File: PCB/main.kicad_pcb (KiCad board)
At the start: 2 copper layers, 82.5 x 58.4 mm, 39 parts, among them CON1 BARREL_JACK, P1 JUMPER_LEFT, P2 LEFT, P3 JUMPER_RIGHT, P4 RIGHT, Q1 3904, Q2 3904, Q3 3904, Q4 3904, SW1 12x12_PUSHBUTTON_SPST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

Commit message: pcb powa!
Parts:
- added REF**: Logo1, myparts:Logo1, F.Cu at (127.0, 52.8)
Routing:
- added copper zone on B.Cu, net GND

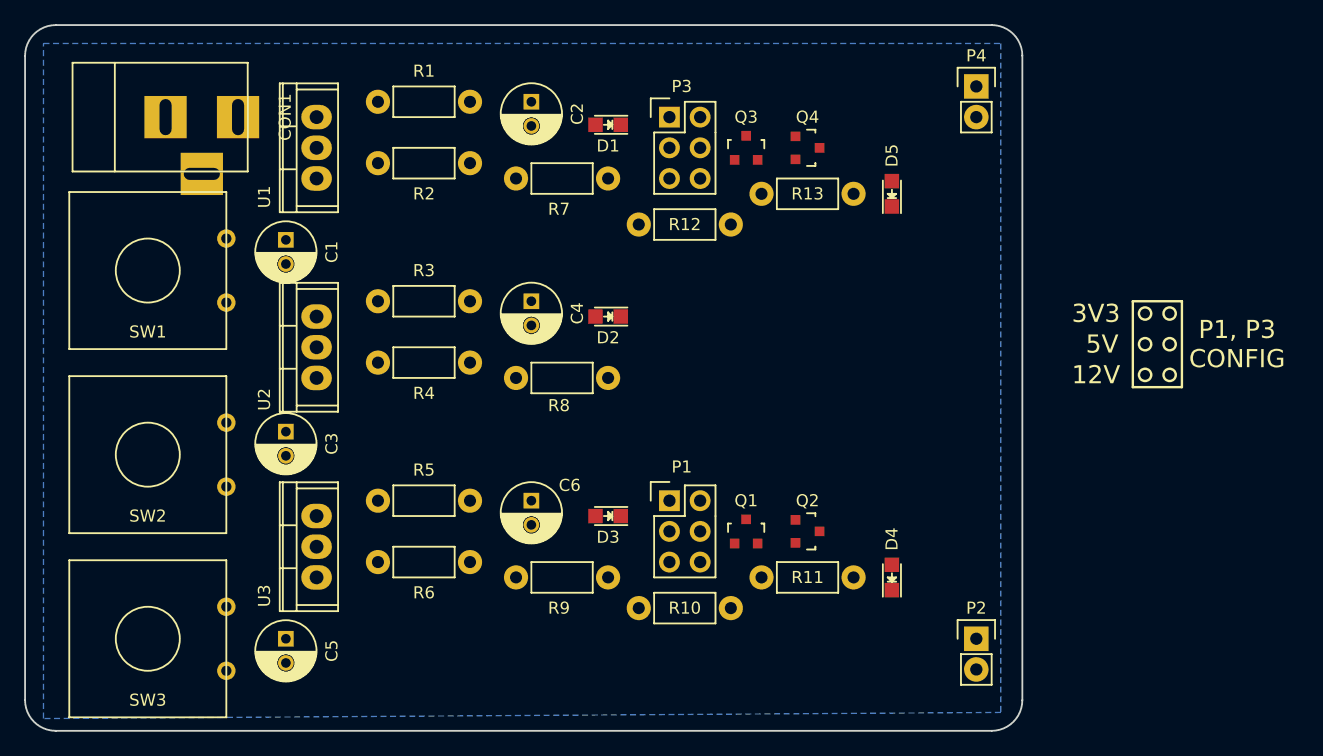
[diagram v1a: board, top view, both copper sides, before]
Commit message: smaller pcb
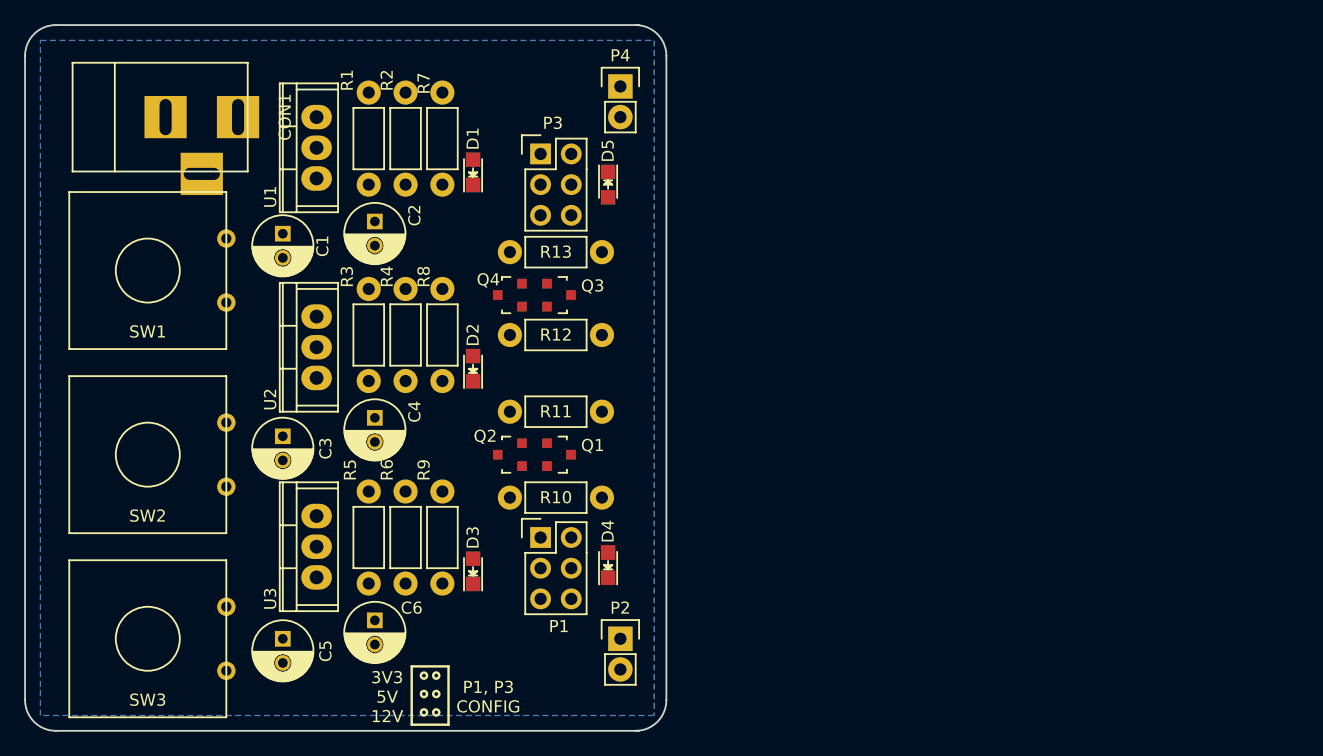
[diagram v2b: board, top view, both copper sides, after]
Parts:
- removed REF**: Logo1, myparts:Logo1
- moved P2 29.5 mm to (102.6, 71.1)
- moved P4 29.5 mm to (102.6, 25.4)
- moved Q4 27.5 mm to (93.5, 42.7), turned to 90 degrees
- moved Q2 25.4 mm to (93.5, 55.9), turned to 90 degrees
- moved D4 23.5 mm to (101.6, 65.0)
- moved D5 23.5 mm to (101.6, 33.5), turned to 270 degrees
- moved R12 20.4 mm to (93.5, 46.0), turned to 0 degrees
- moved Q3 19.7 mm to (97.5, 42.7), turned to 270 degrees
- moved R11 19.0 mm to (101.1, 52.3), turned to 180 degrees
- moved Q1 16.7 mm to (97.5, 55.9), turned to 270 degrees
- moved C6 16.3 mm to (82.3, 69.6)
- moved C2 16.3 mm to (82.3, 36.6)
- moved C4 16.2 mm to (82.3, 52.8)
- moved R13 14.1 mm to (101.1, 39.1), turned to 180 degrees
- moved R10 14.1 mm to (93.5, 59.4)
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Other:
- board size 82.5 x 58.4 mm -> 53.1 x 58.4 mm
- board text added: "3V3 5V 12V"
- board text removed: "12V"
- board text removed: "3V3"
- board text removed: "5V"

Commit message: edge cut fix
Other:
- outline, holes or cut-outs redrawn
- board text added: "+ -"
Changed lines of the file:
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@@
     (area 53.264999 20.244999 106.501001 78.815001)
     (thickness 1.524)
-    (drawings 21)
+    (drawings 23)
     (tracks 0)
     (zones 0)
@@
       (net 6 "Net-(C5-Pad1)"))
   )
+  (gr_text "+\n-" (at 105.156 26.416) (layer F.SilkS)
+    (effects (font (size 1.5 1.5) (thickness 0.3)))
+  )
+  (gr_text "+\n-" (at 105.156 72.39) (layer F.SilkS)
+    (effects (font (size 1.5 1.5) (thickness 0.3)))
+  )
+  (gr_line (start 53.34 22.86) (end 53.34 76.2) (angle 90) (layer Edge.Cuts) (width 0.15))
+  (gr_line (start 106.426 76.2) (end 106.426 22.86) (angle 90) (layer Edge.Cuts) (width 0.15))
+  (gr_line (start 55.88 78.74) (end 103.886 78.74) (angle 90) (layer Edge.Cuts) (width 0.15))
+  (gr_line (start 55.88 20.32) (end 103.886 20.32) (angle 90) (layer Edge.Cuts) (width 0.15))
   (gr_text "P1, P3\nCONFIG" (at 91.694 75.946) (layer F.SilkS)
     (effects (font (size 1 1) (thickness 0.2)))
@@
     (effects (font (size 1 1) (thickness 0.2)))
   )
-  (gr_line (start 55.88 78.74) (end 104.14 78.74) (angle 90) (layer Edge.Cuts) (width 0.15))
-  (gr_line (start 106.426 76.2) (end 106.426 22.86) (angle 90) (layer Edge.Cuts) (width 0.15))
-  (gr_line (start 55.88 20.32) (end 104.14 20.32) (angle 90) (layer Edge.Cuts) (width 0.15))
   (gr_text "Breadboard Power Supply v0.1\nBy : Yannick Gagne" (at 60.452 54.864 90) (layer B.SilkS)
     (effects (font (size 1.5 1.5) (thickness 0.3)) (justify mirror))
   )
-  (gr_line (start 53.34 22.86) (end 53.34 76.2) (angle 90) (layer Edge.Cuts) (width 0.15))
   (gr_arc (start 103.886 22.86) (end 103.886 20.32) (angle 90) (layer Edge.Cuts) (width 0.15))
   (gr_arc (start 103.886 76.2) (end 106.426 76.2) (angle 90) (layer Edge.Cuts) (width 0.15))

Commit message: output pins
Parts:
- moved P4 2.54 mm to (102.6, 27.9), turned to 180 degrees
- moved P2 2.54 mm to (102.6, 73.7), turned to 180 degrees
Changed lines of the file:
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@@
   (layers
     (0 F.Cu signal)
-    (31 B.Cu signal hide)
+    (31 B.Cu signal)
     (34 B.Paste user)
     (35 F.Paste user)
@@
       (effects (font (size 1 1) (thickness 0.15)))
     )
-    (fp_text value JUMPER_LEFT (at 1.016 8.89) (layer F.Fab) hide
+    (fp_text value JUMPER_LEFT (at 0 8.89) (layer F.Fab) hide
       (effects (font (size 1 1) (thickness 0.15)))
     )
@@
   )
   (module Pin_Headers:Pin_Header_Straight_1x02 (layer F.Cu)
-    (at 102.616 71.12)
+    (at 102.616 73.66 180)
     (descr "Through hole pin header")
     (tags "pin header")
-    (fp_text reference P2 (at 0 -2.54) (layer F.SilkS)
-      (effects (font (size 1 1) (thickness 0.15)))
-    )
-    (fp_text value LEFT (at 0 5.08) (layer F.Fab) hide
+    (fp_text reference P2 (at 0 -2.54 180) (layer F.SilkS)
+      (effects (font (size 1 1) (thickness 0.15)))
+    )
+    (fp_text value LEFT (at 0 5.08 180) (layer F.Fab) hide
       (effects (font (size 1 1) (thickness 0.15)))
     )
@@
     (fp_line (start -1.27 1.27) (end -1.27 3.81) (layer F.SilkS) (width 0.15))
     (fp_line (start -1.27 3.81) (end 1.27 3.81) (layer F.SilkS) (width 0.15))
-    (pad 1 thru_hole rect (at 0 0) (size 2.032 2.032) (drill 1.016) (layers *.Cu *.Mask F.SilkS)
+    (pad 1 thru_hole rect (at 0 0 180) (size 2.032 2.032) (drill 1.016) (layers *.Cu *.Mask F.SilkS)
       (net 15 "Net-(P1-Pad2)"))
-    (pad 2 thru_hole oval (at 0 2.54) (size 2.032 2.032) (drill 1.016) (layers *.Cu *.Mask F.SilkS)
+    (pad 2 thru_hole oval (at 0 2.54 180) (size 2.032 2.032) (drill 1.016) (layers *.Cu *.Mask F.SilkS)
       (net 2 GND))
     (model Pin_Headers.3dshapes/Pin_Header_Straight_1x02.wrl
@@
   )
   (module Pin_Headers:Pin_Header_Straight_1x02 (layer F.Cu)
-    (at 102.616 25.4)
+    (at 102.616 27.94 180)
     (descr "Through hole pin header")
     (tags "pin header")
-    (fp_text reference P4 (at 0 -2.54) (layer F.SilkS)
-      (effects (font (size 1 1) (thickness 0.15)))
-    )
-    (fp_text value RIGHT (at 0 5.588) (layer F.Fab) hide
+    (fp_text reference P4 (at 0 -2.54 180) (layer F.SilkS)
+      (effects (font (size 1 1) (thickness 0.15)))
+    )
+    (fp_text value RIGHT (at 0 5.588 180) (layer F.Fab) hide
       (effects (font (size 1 1) (thickness 0.15)))
     )
@@
     (fp_line (start -1.27 1.27) (end -1.27 3.81) (layer F.SilkS) (width 0.15))
     (fp_line (start -1.27 3.81) (end 1.27 3.81) (layer F.SilkS) (width 0.15))
-    (pad 1 thru_hole rect (at 0 0) (size 2.032 2.032) (drill 1.016) (layers *.Cu *.Mask F.SilkS)
+    (pad 1 thru_hole rect (at 0 0 180) (size 2.032 2.032) (drill 1.016) (layers *.Cu *.Mask F.SilkS)
       (net 16 "Net-(P3-Pad2)"))
-    (pad 2 thru_hole oval (at 0 2.54) (size 2.032 2.032) (drill 1.016) (layers *.Cu *.Mask F.SilkS)
+    (pad 2 thru_hole oval (at 0 2.54 180) (size 2.032 2.032) (drill 1.016) (layers *.Cu *.Mask F.SilkS)
       (net 2 GND))
     (model Pin_Headers.3dshapes/Pin_Header_Straight_1x02.wrl
@@
       (net 6 "Net-(C5-Pad1)"))
   )
-  (gr_text "+\n-" (at 105.156 26.416) (layer F.SilkS)
+  (gr_text "+\n-" (at 105.156 26.67 180) (layer F.SilkS)
     (effects (font (size 1.5 1.5) (thickness 0.3)))
   )
-  (gr_text "+\n-" (at 105.156 72.39) (layer F.SilkS)
+  (gr_text "+\n-" (at 105.156 72.39 180) (layer F.SilkS)
     (effects (font (size 1.5 1.5) (thickness 0.3)))
   )

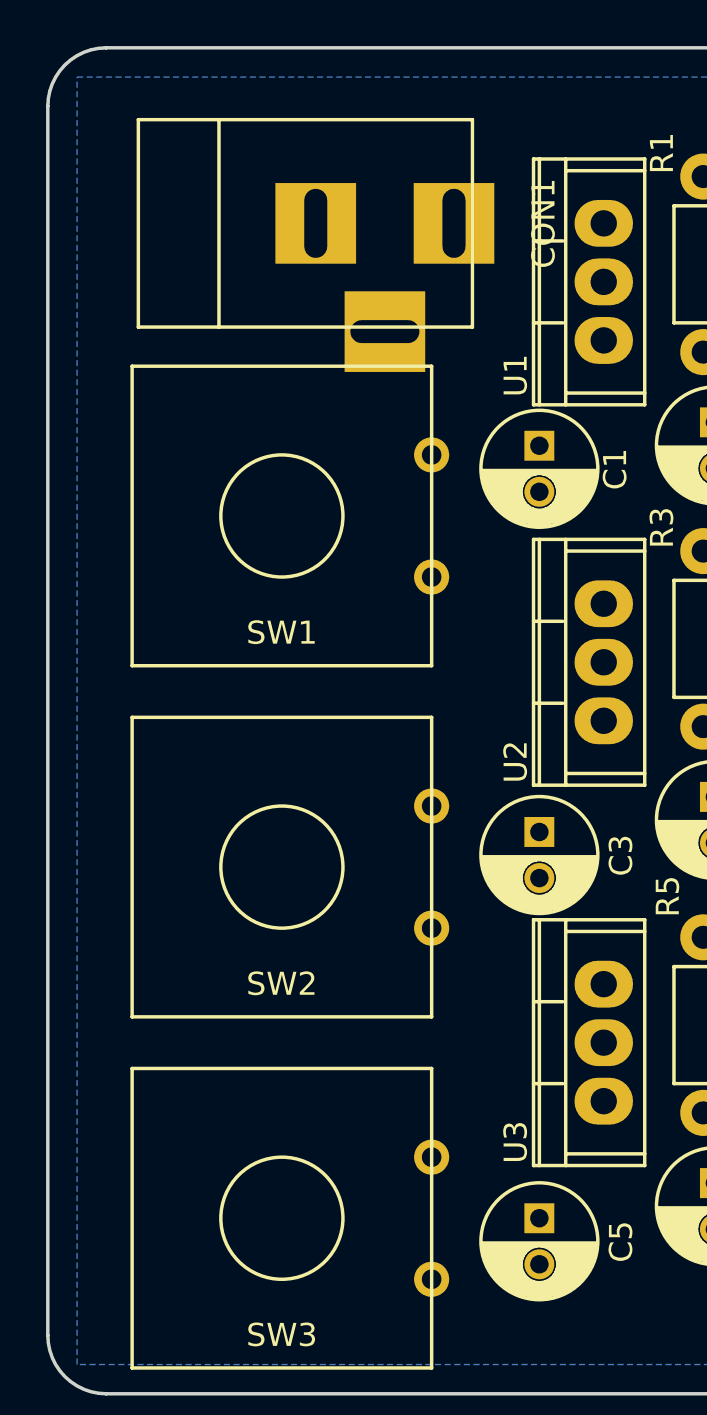
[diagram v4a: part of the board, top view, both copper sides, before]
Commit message: added to top silk screen
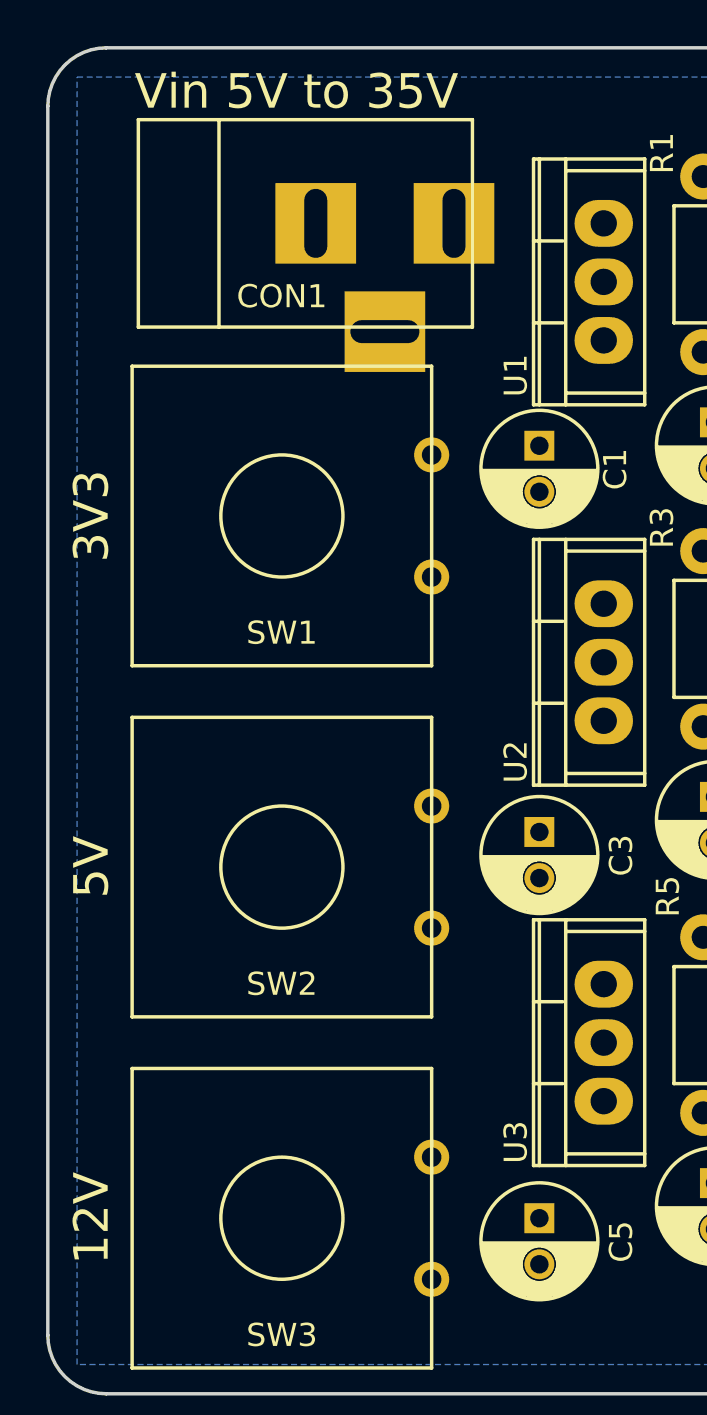
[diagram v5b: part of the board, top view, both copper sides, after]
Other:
- board text added: "12V"
- board text added: "3V3"
- board text added: "5V"
- board text added: "Vin 5V to 35V"
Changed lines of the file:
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@@
     (area 53.264999 20.244999 106.501001 78.815001)
     (thickness 1.524)
-    (drawings 23)
+    (drawings 28)
     (tracks 0)
     (zones 0)
@@
   (layers
     (0 F.Cu signal)
-    (31 B.Cu signal)
+    (31 B.Cu signal hide)
     (34 B.Paste user)
     (35 F.Paste user)
@@
     (descr "DC Barrel Jack")
     (tags "Power Jack")
-    (fp_text reference CON1 (at 10.09904 0 90) (layer F.SilkS)
-      (effects (font (size 1 1) (thickness 0.15)))
-    )
-    (fp_text value BARREL_JACK (at 1.27 -2.54) (layer F.Fab)
+    (fp_text reference CON1 (at -1.27 3.175 180) (layer F.SilkS)
+      (effects (font (size 1 1) (thickness 0.15)))
+    )
+    (fp_text value BARREL_JACK (at 1.27 -2.54) (layer F.Fab) hide
       (effects (font (size 1 1) (thickness 0.15)))
     )
@@
       (net 6 "Net-(C5-Pad1)"))
   )
+  (dimension 48.26 (width 0.3) (layer F.SilkS)
+    (gr_text "48,260 mm" (at 115.65 49.53 270) (layer F.SilkS)
+      (effects (font (size 1.5 1.5) (thickness 0.3)))
+    )
+    (feature1 (pts (xy 108.585 73.66) (xy 117 73.66)))
+    (feature2 (pts (xy 108.585 25.4) (xy 117 25.4)))
+    (crossbar (pts (xy 114.3 25.4) (xy 114.3 73.66)))
+    (arrow1a (pts (xy 114.3 73.66) (xy 113.713579 72.533496)))
+    (arrow1b (pts (xy 114.3 73.66) (xy 114.886421 72.533496)))
+    (arrow2a (pts (xy 114.3 25.4) (xy 113.713579 26.526504)))
+    (arrow2b (pts (xy 114.3 25.4) (xy 114.886421 26.526504)))
+  )
+  (gr_text "Vin 5V to 35V" (at 64.135 22.225) (layer F.SilkS)
+    (effects (font (size 1.5 1.5) (thickness 0.3)))
+  )
+  (gr_text 12V (at 55.245 71.12 90) (layer F.SilkS)
+    (effects (font (size 1.5 1.5) (thickness 0.3)))
+  )
+  (gr_text 5V (at 55.245 55.88 90) (layer F.SilkS)
+    (effects (font (size 1.5 1.5) (thickness 0.3)))
+  )
+  (gr_text 3V3 (at 55.245 40.64 90) (layer F.SilkS)
+    (effects (font (size 1.5 1.5) (thickness 0.3)))
+  )
   (gr_text "+\n-" (at 105.156 26.67 180) (layer F.SilkS)

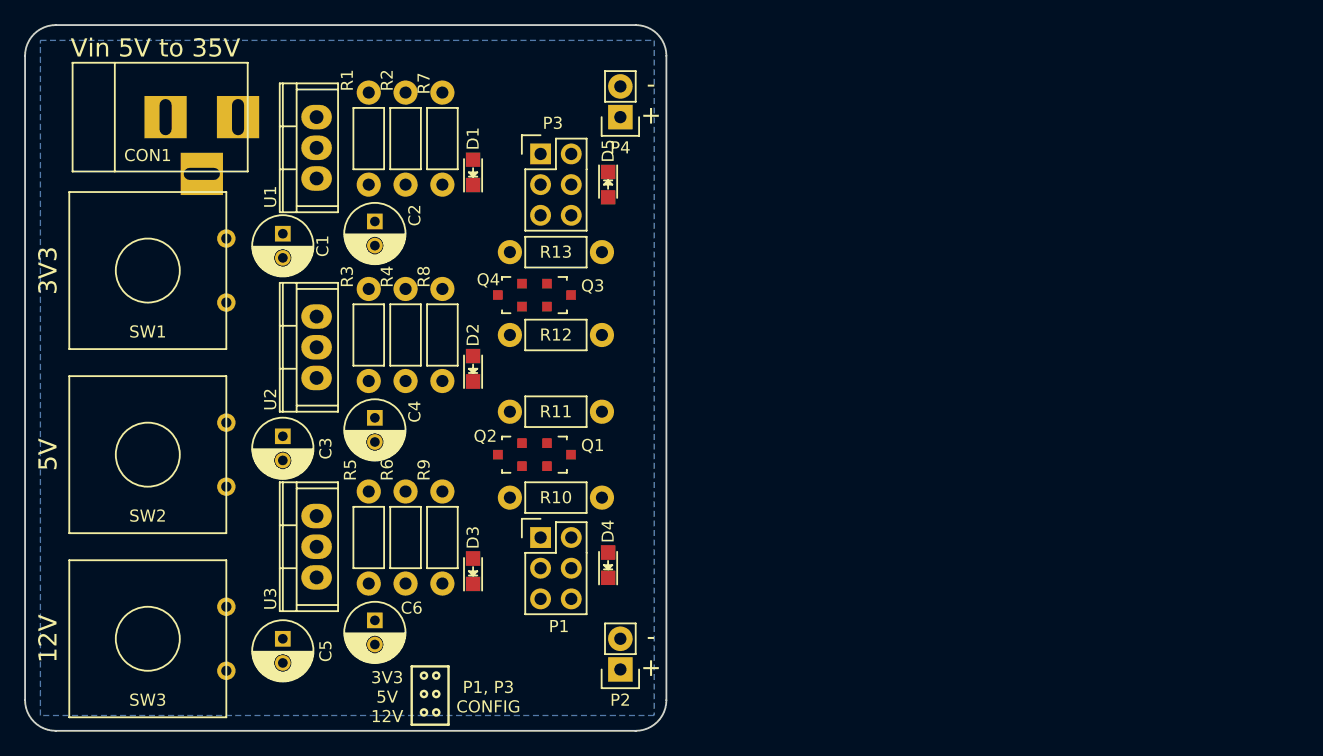
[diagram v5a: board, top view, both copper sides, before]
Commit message: fat holes for barrel jack
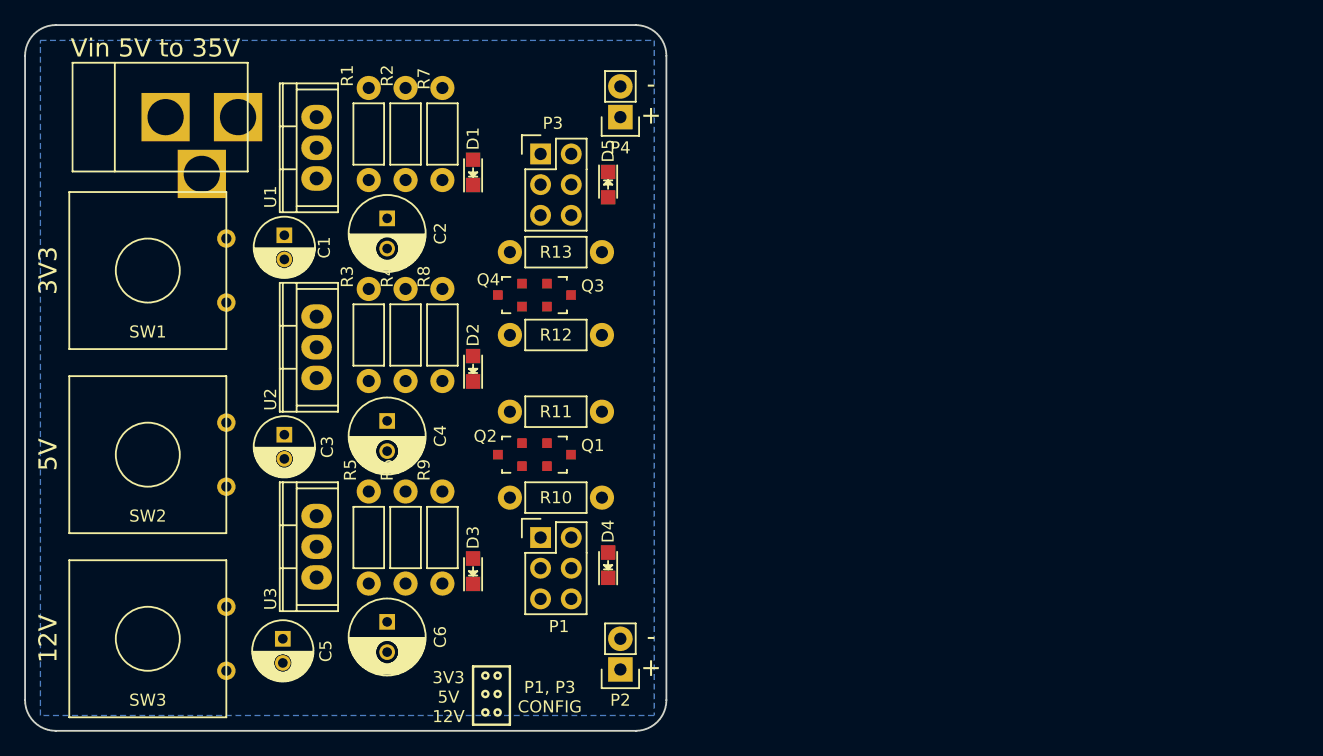
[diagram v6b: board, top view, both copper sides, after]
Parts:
- C2, C4, C6: footprint Capacitors_ThroughHole:C_Radial_D5_L11_P2 -> Capacitors_ThroughHole:C_Radial_D6.3_L11.2_P2.5
- CON1: footprint Connect:BARREL_JACK -> mods:BARREL_JACK2
- moved C2 1.05 mm to (83.3, 36.3)
- moved C4 1.05 mm to (83.3, 53.1)
- moved C6 1.02 mm to (83.3, 69.7)
- moved R1 0.38 mm to (81.8, 33.1)
- moved R2 0.38 mm to (84.8, 25.5)
- moved R7 0.38 mm to (87.9, 33.1)
- moved C1 0.18 mm to (74.8, 37.7)
- moved C3 0.18 mm to (74.8, 54.2)

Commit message: hopefully last pcb layout
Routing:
- net +3V3: track 0.00 -> 88.0 mm
- net +12V: track 0.00 -> 75.8 mm
- net +5V: track 0.00 -> 55.2 mm
- net Net-(CON1-Pad1): track 0.00 -> 44.4 mm
- net Net-(P1-Pad2): track 0.00 -> 24.1 mm, vias 0 -> 1
- net Net-(D4-Pad2): track 0.00 -> 21.8 mm, vias 0 -> 1
- net Net-(P3-Pad2): track 0.00 -> 21.4 mm
- net Net-(C1-Pad1): track 0.00 -> 19.2 mm
- net Net-(C3-Pad1): track 0.00 -> 17.5 mm
- net Net-(C5-Pad1): track 0.00 -> 17.1 mm
- net Net-(R1-Pad2): track 0.00 -> 13.1 mm
- net Net-(D5-Pad2): track 0.00 -> 13.1 mm, vias 0 -> 1
- net Net-(R3-Pad2): track 0.00 -> 12.6 mm
- net Net-(R5-Pad2): track 0.00 -> 12.4 mm
- net Net-(Q3-Pad1): track 0.00 -> 11.2 mm
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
